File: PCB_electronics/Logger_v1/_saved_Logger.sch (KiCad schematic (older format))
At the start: 26 parts, among them P1 GPS_breakout_connector, P10 CONN_01X03, P11 CONN_01X02, P12 CONN_01X02, P13 CONN_01X02, P14 CONN_01X02, P15 CONN_01X02, P2 SD_breakout_connector, P3 Iridium_connector, P4 VN100_connector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

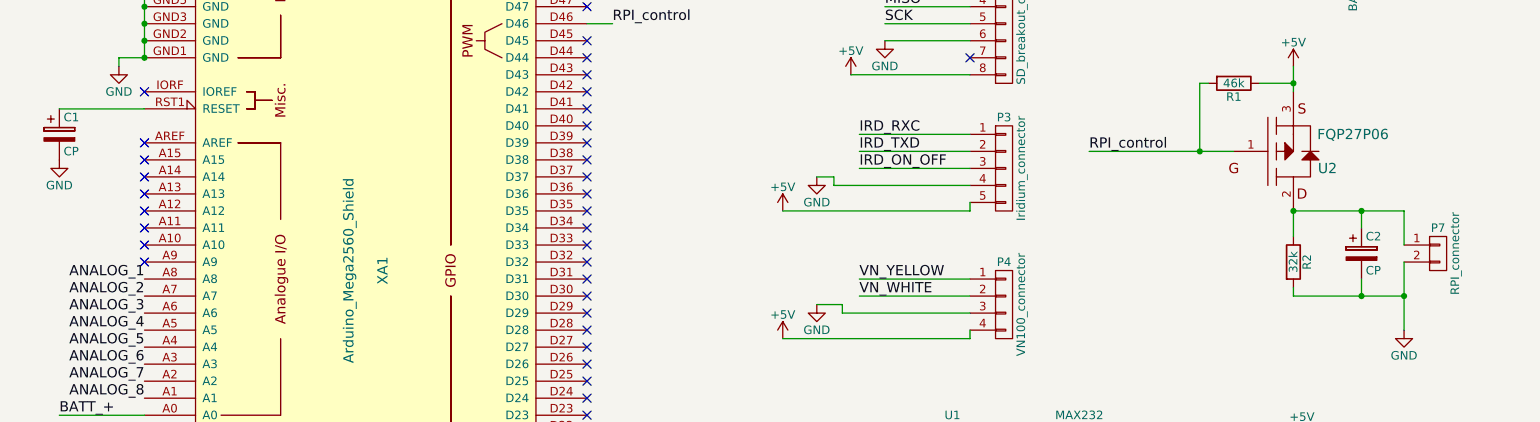
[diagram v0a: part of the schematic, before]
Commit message: placed components 1
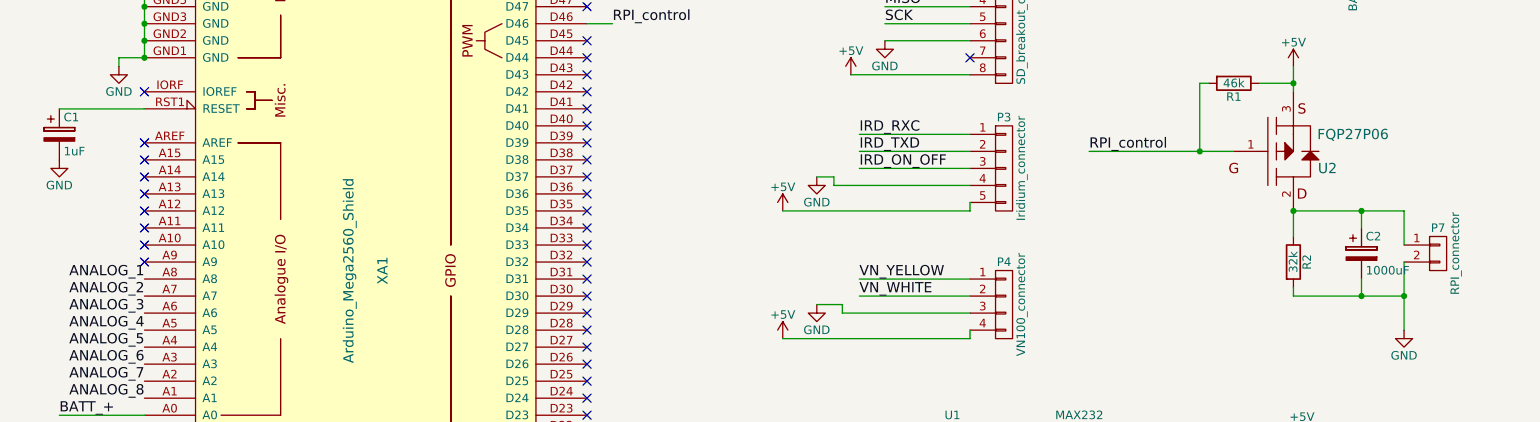
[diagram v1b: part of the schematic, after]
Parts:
- C1: value CP -> 1uF; footprint (none) -> Capacitors_ThroughHole:C_Radial_D8_L11.5_P3.5
- C2: value CP -> 1000uF; footprint (none) -> Capacitors_ThroughHole:C_Radial_D8_L13_P3.8
- C3, C4, C5, C6: footprint (none) -> Capacitors_ThroughHole:C_Disc_D3_P2.5
- P1: footprint (none) -> Pin_Headers:Pin_Header_Straight_1x09
- P10, P5: footprint (none) -> Pin_Headers:Pin_Header_Straight_1x03
- P11, P12, P13, P14, P15, P7: footprint (none) -> Pin_Headers:Pin_Header_Straight_2x01
- P2, P8, P9: footprint (none) -> Pin_Headers:Pin_Header_Straight_1x08
- P3: footprint (none) -> Pin_Headers:Pin_Header_Straight_1x05
- P4: footprint (none) -> Pin_Headers:Pin_Header_Straight_1x04
- P6: footprint (none) -> Pin_Headers:Pin_Header_Straight_1x01
- R1, R2: footprint (none) -> Resistors_ThroughHole:Resistor_Horizontal_RM10mm
- U1: footprint (none) -> Housings_DIP:DIP-16_W7.62mm_LongPads
- U2: footprint (none) -> TO_SOT_Packages_THT:TO-220_Neutral123_Vertical
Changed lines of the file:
@@
 F 0 "P1" H 6350 1650 50  0000 C CNN
 F 1 "GPS_breakout_connector" V 6450 1150 50  0000 C CNN
-F 2 "" H 6350 1150 50  0000 C CNN
+F 2 "Pin_Headers:Pin_Header_Straight_1x09" H 6350 1150 50  0001 C CNN
 F 3 "" H 6350 1150 50  0000 C CNN
 	1    6350 1150
@@
 F 0 "P2" H 6350 2700 50  0000 C CNN
 F 1 "SD_breakout_connector" V 6450 2250 50  0000 C CNN
-F 2 "" H 6350 2250 50  0000 C CNN
+F 2 "Pin_Headers:Pin_Header_Straight_1x08" H 6350 2250 50  0001 C CNN
 F 3 "" H 6350 2250 50  0000 C CNN
 	1    6350 2250
@@
 F 0 "U1" H 6000 6300 50  0000 L CNN
 F 1 "MAX232" H 6650 6300 50  0000 L CNN
-F 2 "" H 6450 5450 50  0000 C CNN
+F 2 "Housings_DIP:DIP-16_W7.62mm_LongPads" H 6450 5450 50  0001 C CNN
 F 3 "" H 6450 5450 50  0000 C CNN
 	1    6450 5450
@@
 F 0 "U2" H 8250 2950 60  0000 C CNN
 F 1 "FQP27P06" H 8400 3150 60  0000 C CNN
-F 2 "" H 8050 3050 60  0000 C CNN
+F 2 "TO_SOT_Packages_THT:TO-220_Neutral123_Vertical" H 8050 3050 60  0001 C CNN
 F 3 "" H 8050 3050 60  0000 C CNN
 	1    8050 3050
@@
 P 800 2950
 F 0 "C1" H 825 3050 50  0000 L CNN
-F 1 "CP" H 825 2850 50  0000 L CNN
-F 2 "" H 838 2800 50  0000 C CNN
+F 1 "1uF" H 825 2850 50  0000 L CNN
+F 2 "Capacitors_ThroughHole:C_Radial_D8_L11.5_P3.5" H 838 2800 50  0001 C CNN
 F 3 "" H 800 2950 50  0000 C CNN
 	1    800  2950
@@
 F 0 "P4" H 6350 4200 50  0000 C CNN
 F 1 "VN100_connector" V 6450 3950 50  0000 C CNN
-F 2 "" H 6350 3950 50  0000 C CNN
+F 2 "Pin_Headers:Pin_Header_Straight_1x04" H 6350 3950 50  0001 C CNN
 F 3 "" H 6350 3950 50  0000 C CNN
 	1    6350 3950
@@
 F 0 "P7" H 8900 3800 50  0000 C CNN
 F 1 "RPI_connector" V 9000 3650 50  0000 C CNN
-F 2 "" H 8900 3650 50  0000 C CNN
+F 2 "Pin_Headers:Pin_Header_Straight_2x01" H 8900 3650 50  0001 C CNN
 F 3 "" H 8900 3650 50  0000 C CNN
 	1    8900 3650
@@
 F 0 "P5" H 8300 1300 50  0000 C CNN
 F 1 "PowerManager_connector" V 8400 1100 50  0000 C CNN
-F 2 "" H 8300 1100 50  0000 C CNN
+F 2 "Pin_Headers:Pin_Header_Straight_1x03" H 8300 1100 50  0001 C CNN
 F 3 "" H 8300 1100 50  0000 C CNN
 	1    8300 1100
@@
 F 0 "P3" H 6350 3450 50  0000 C CNN
 F 1 "Iridium_connector" V 6450 3150 50  0000 C CNN
-F 2 "" H 6350 3150 50  0000 C CNN
+F 2 "Pin_Headers:Pin_Header_Straight_1x05" H 6350 3150 50  0001 C CNN
 F 3 "" H 6350 3150 50  0000 C CNN
 	1    6350 3150
@@
 F 0 "P6" H 8300 2050 50  0000 C CNN
 F 1 "BATT_connector" V 8400 1950 50  0000 C CNN
-F 2 "" H 8300 1950 50  0000 C CNN
+F 2 "Pin_Headers:Pin_Header_Straight_1x01" H 8300 1950 50  0001 C CNN
 F 3 "" H 8300 1950 50  0000 C CNN
 	1    8300 1950
@@
 P 8450 3650
 F 0 "C2" H 8475 3750 50  0000 L CNN
-F 1 "CP" H 8475 3550 50  0000 L CNN
-F 2 "" H 8488 3500 50  0000 C CNN
+F 1 "1000uF" H 8475 3550 50  0000 L CNN
+F 2 "Capacitors_ThroughHole:C_Radial_D8_L13_P3.8" H 8488 3500 50  0001 C CNN
 F 3 "" H 8450 3650 50  0000 C CNN
 	1    8450 3650
@@
 F 0 "R1" V 7780 2650 50  0000 C CNN
 F 1 "46k" V 7700 2650 50  0000 C CNN
-F 2 "" V 7630 2650 50  0000 C CNN
+F 2 "Resistors_ThroughHole:Resistor_Horizontal_RM10mm" V 7630 2650 50  0001 C CNN
 F 3 "" H 7700 2650 50  0000 C CNN
 	1    7700 2650
@@
 F 0 "R2" V 8130 3700 50  0000 C CNN
 F 1 "32k" V 8050 3700 50  0000 C CNN
-F 2 "" V 7980 3700 50  0000 C CNN
+F 2 "Resistors_ThroughHole:Resistor_Horizontal_RM10mm" V 7980 3700 50  0001 C CNN
 F 3 "" H 8050 3700 50  0000 C CNN
 	1    8050 3700
@@
 F 0 "P8" H 10450 1700 50  0000 C CNN
 F 1 "CONN_01X08" V 10550 1250 50  0000 C CNN
-F 2 "" H 10450 1250 50  0000 C CNN
+F 2 "Pin_Headers:Pin_Header_Straight_1x08" H 10450 1250 50  0001 C CNN
 F 3 "" H 10450 1250 50  0000 C CNN
 	1    10450 1250
@@
 F 0 "P9" H 10450 2800 50  0000 C CNN
 F 1 "CONN_01X08" V 10550 2350 50  0000 C CNN
-F 2 "" H 10450 2350 50  0000 C CNN
+F 2 "Pin_Headers:Pin_Header_Straight_1x08" H 10450 2350 50  0001 C CNN
 F 3 "" H 10450 2350 50  0000 C CNN
 	1    10450 2350
@@
 F 0 "P10" H 10450 3400 50  0000 C CNN
 F 1 "CONN_01X03" V 10550 3200 50  0000 C CNN
-F 2 "" H 10450 3200 50  0000 C CNN
+F 2 "Pin_Headers:Pin_Header_Straight_1x03" H 10450 3200 50  0001 C CNN
 F 3 "" H 10450 3200 50  0000 C CNN
 	1    10450 3200
@@
 F 0 "P11" H 10450 4000 50  0000 C CNN
 F 1 "CONN_01X02" V 10550 3850 50  0000 C CNN
-F 2 "" H 10450 3850 50  0000 C CNN
+F 2 "Pin_Headers:Pin_Header_Straight_2x01" H 10450 3850 50  0001 C CNN
 F 3 "" H 10450 3850 50  0000 C CNN
 	1    10450 3850
@@
 F 0 "P13" H 10450 5250 50  0000 C CNN
 F 1 "CONN_01X02" V 10550 5100 50  0000 C CNN
-F 2 "" H 10450 5100 50  0000 C CNN
+F 2 "Pin_Headers:Pin_Header_Straight_2x01" H 10450 5100 50  0001 C CNN
 F 3 "" H 10450 5100 50  0000 C CNN
 	1    10450 5100
@@
 F 0 "C3" H 5475 5050 50  0000 L CNN
 F 1 "1.0uF" H 5475 4850 50  0000 L CNN
-F 2 "" H 5488 4800 50  0000 C CNN
+F 2 "Capacitors_ThroughHole:C_Disc_D3_P2.5" H 5488 4800 50  0001 C CNN
 F 3 "" H 5450 4950 50  0000 C CNN
 	1    5450 4950
@@
 F 0 "C4" H 5475 5550 50  0000 L CNN
 F 1 "1.0uF" H 5475 5350 50  0000 L CNN
-F 2 "" H 5488 5300 50  0000 C CNN
+F 2 "Capacitors_ThroughHole:C_Disc_D3_P2.5" H 5488 5300 50  0001 C CNN
 F 3 "" H 5450 5450 50  0000 C CNN
 	1    5450 5450
@@
 F 0 "C5" H 7425 5250 50  0000 L CNN
 F 1 "1.0uF" V 7250 5050 50  0000 L CNN
-F 2 "" H 7438 5000 50  0000 C CNN
+F 2 "Capacitors_ThroughHole:C_Disc_D3_P2.5" H 7438 5000 50  0001 C CNN
 F 3 "" H 7400 5150 50  0000 C CNN
 	1    7400 5150
@@
 F 0 "C6" H 7425 5750 50  0000 L CNN
 F 1 "1.0uF" V 7250 5550 50  0000 L CNN
-F 2 "" H 7438 5500 50  0000 C CNN
+F 2 "Capacitors_ThroughHole:C_Disc_D3_P2.5" H 7438 5500 50  0001 C CNN
 F 3 "" H 7400 5650 50  0000 C CNN
 	1    7400 5650
@@
 F 0 "P12" H 10450 4600 50  0000 C CNN
 F 1 "CONN_01X02" V 10550 4450 50  0000 C CNN
-F 2 "" H 10450 4450 50  0000 C CNN
+F 2 "Pin_Headers:Pin_Header_Straight_2x01" H 10450 4450 50  0001 C CNN
 F 3 "" H 10450 4450 50  0000 C CNN
 	1    10450 4450
@@
 F 0 "P14" H 4900 6500 50  0000 C CNN
 F 1 "CONN_01X02" V 5000 6350 50  0000 C CNN
-F 2 "" H 4900 6350 50  0000 C CNN
+F 2 "Pin_Headers:Pin_Header_Straight_2x01" H 4900 6350 50  0001 C CNN
 F 3 "" H 4900 6350 50  0000 C CNN
 	1    4900 6350
@@
 F 0 "P15" H 8350 6400 50  0000 C CNN
 F 1 "CONN_01X02" V 8450 6250 50  0000 C CNN
-F 2 "" H 8350 6250 50  0000 C CNN
+F 2 "Pin_Headers:Pin_Header_Straight_2x01" H 8350 6250 50  0001 C CNN
 F 3 "" H 8350 6250 50  0000 C CNN
 	1    8350 6250
